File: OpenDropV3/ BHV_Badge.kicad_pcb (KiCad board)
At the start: 2 copper layers, 100 x 112 mm, 270 parts, among them J1 USB_C_Receptacle, J2 Conn_02x05_Odd_Even, P1 CONN_01X01, P10 CONN_01X01, P11 CONN_01X01, P12 CONN_01X01, P13 ScrewPad1, P14 ScrewPad2, P15 ScrewPad3, P16 ScrewPad4, P2 ScrewPad4, P3 CONN_01X01, P4 CONN_PSEUDO_AC, P7 CONN_01X01, P8 CONN_01X01, P9 CONN_01X01, SW1 SW_PUSH, SW2 SW_PUSH, SW3 SW_PUSH, SW5 SPST, T1 TK560P60Y, U1 MAX1771ESA, U10 AQY210EH, U11 AQY210EH, U12 AQY210EH, U13 AQY210EH, U14 TLV1117-33, U15 MCP41010, U16 74xx14, U2 HV507, U3 PAM8301, U4 HV507, U5 SAMD21G18B-A changed from SAM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, U6 MCP6002, U7 HCPL0534, U8 HCPL0534, U9 HCPL0534, Y1 32.765

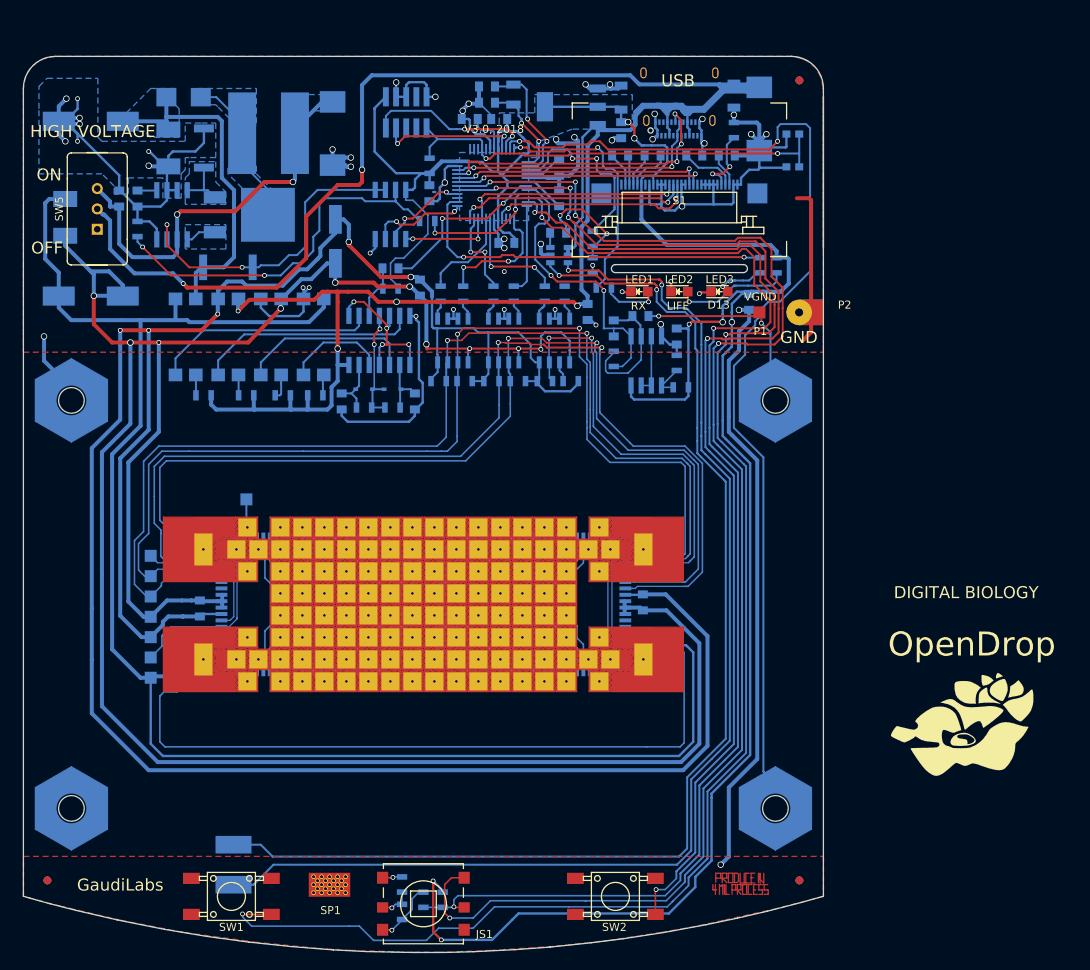
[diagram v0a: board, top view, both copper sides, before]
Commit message: Updated footprints and adjusted copper pour areas
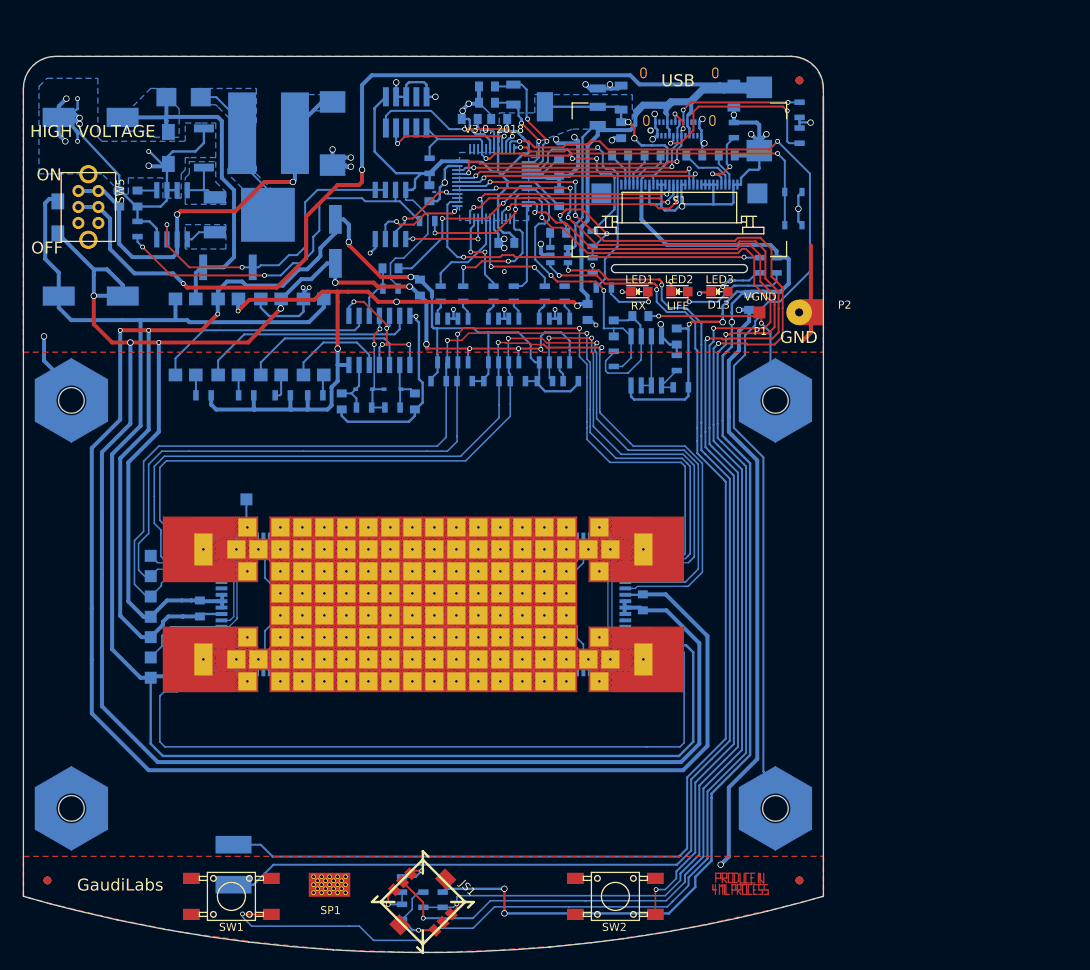
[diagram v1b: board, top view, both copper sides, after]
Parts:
- removed the G*** at (167.5, 114.5)
- added R14: 5R1, Resistors_SMD:R_0805, B.Cu at (147.0, 37.7)
- added R23: 5R1, Resistors_SMD:R_0805, B.Cu at (147.0, 40.9)
- C21, C5: value 10uF -> 22uF
- C32: value 100uF,35V -> 100uF,50V
- C35, C6: footprint GaudiLabsFootPrints:C_1913 -> Capacitors_SMD:C_1206_HandSoldering
- JS1: footprint GaudiLabsFootPrints:JoystickSMD_SKQUSeries -> Solutions:5P_Joystick_SKRHAAE010
- SW3: value SW_PUSH -> PTS810_SJK_250_SMTR_LFS; footprint GaudiLabsFootPrints:SW_SPST_KMS221GLFS -> OpenBCI:PTS810
- SW5: footprint GaudiLabsFootPrints:Switch_On-On -> Solutions:OS202011MA2QS1_DPDT
- moved SW3 6.40 mm to (145.9, 49.1), turned to 270 degrees
- moved SW5 1.13 mm to (58.1, 49.8), turned to 270 degrees
- moved C35 0.93 mm to (54.3, 51.1)
- moved C4 0.49 mm to (58.4, 38.6)
- moved JS1 0.24 mm to (99.9, 136.7), turned to 315 degrees
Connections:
- J1 pad S1: Net-(J1-PadS1) -> GND
- JS1 pad 2: Net-(JS1-Pad2) -> SW3
- JS1 pad 4: GND -> JOY
- JS1 pad 5: JOY -> GND
- JS1 pad 6: SW3 -> Net-(JS1-Pad6)
- R19 pad 1: Net-(JS1-Pad3) -> Net-(JS1-Pad6)
- R20 pad 1: Net-(JS1-Pad2) -> Net-(JS1-Pad3)
- R20 pad 2: Net-(JS1-Pad3) -> Net-(JS1-Pad6)
- R21 pad 2: Net-(JS1-Pad2) -> Net-(JS1-Pad3)
- SW3 pad 2: GND -> RESET
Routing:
- net Net-(J1-PadA5): track 0.00 -> 24.6 mm, vias 0 -> 2
- net Net-(J1-PadB5): track 0.00 -> 16.5 mm, vias 0 -> 2
- net Net-(JS1-Pad6): track 0.00 -> 9.60 mm, vias 0 -> 1
- net +3V3: track 304.8 -> 297.0 mm
- net SENS_PAD: track 131.0 -> 124.9 mm
- net V_USB: track 301.1 -> 295.2 mm
- net Net-(JS1-Pad2): track 4.17 -> 0.00 mm, vias 1 -> 0
- net GND: track 365.8 -> 362.0 mm, vias 48 -> 50
- net Net-(JS1-Pad3): track 7.91 -> 5.41 mm
- net RESET: track 56.8 -> 59.2 mm
- net Net-(C1-Pad1): track 50.9 -> 52.8 mm
- net Net-(JS1-Pad1): track 2.48 -> 4.33 mm
- net SW3: track 176.7 -> 178.4 mm
- net V_HV_C: track 212.7 -> 211.8 mm
- net D-: track 37.8 -> 36.9 mm
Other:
- board text removed: "DIGITAL BIOLOGY"
- board text removed: "OpenDrop"

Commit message: Change to pcb file
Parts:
- removed the G*** at (127.9, 131.9)
- added G***: LOGO, Solutions:BHVL, F.Cu at (99.8, 46.4)
- added G***: LOGO, GaudiLabsLogos:LOGO, B.Cu at (134.2, 82.1)
- moved REF*** 8.10 mm to (135.1, 114.9)
- moved G*** 7.38 mm to (137.3, 106.1)
- moved G*** 7.14 mm to (139.2, 98.0)
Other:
- board size 100 x 112 mm -> 100 x 117 mm
- board text added: "BIOHACKING VILLAGE DEF CON 26"
- board text added: "BioHacking Village Badge for Def Con 26 Produced by Joel Murphy = biomurph Based on OpenDrop"
- board text added: "OpenDrop"
